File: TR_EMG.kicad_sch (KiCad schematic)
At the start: 20 parts, among them U1 INA115BU, U2 LM2904DR, U3 LM2904DR

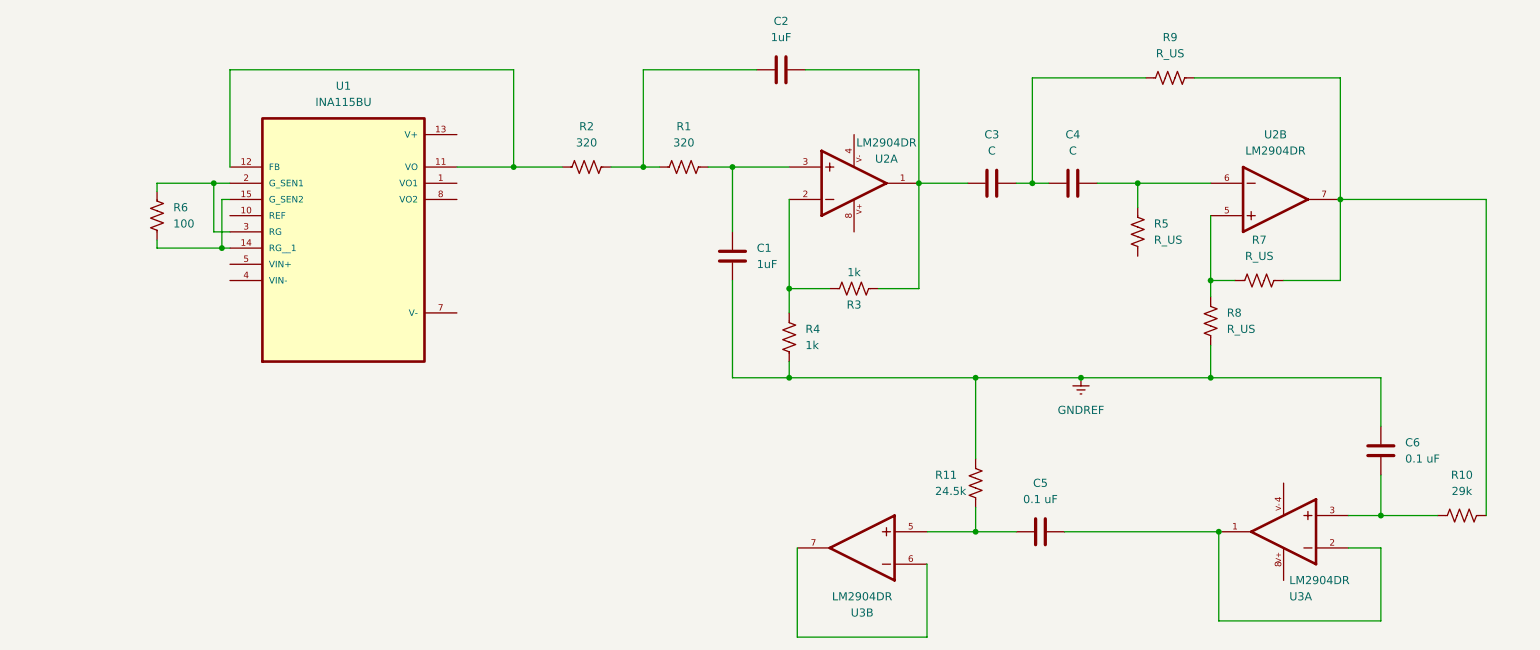
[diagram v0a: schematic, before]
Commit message: Added Hierarchy to initial design
Added hierarchy for the 2nd order lowpass and the band stop filter
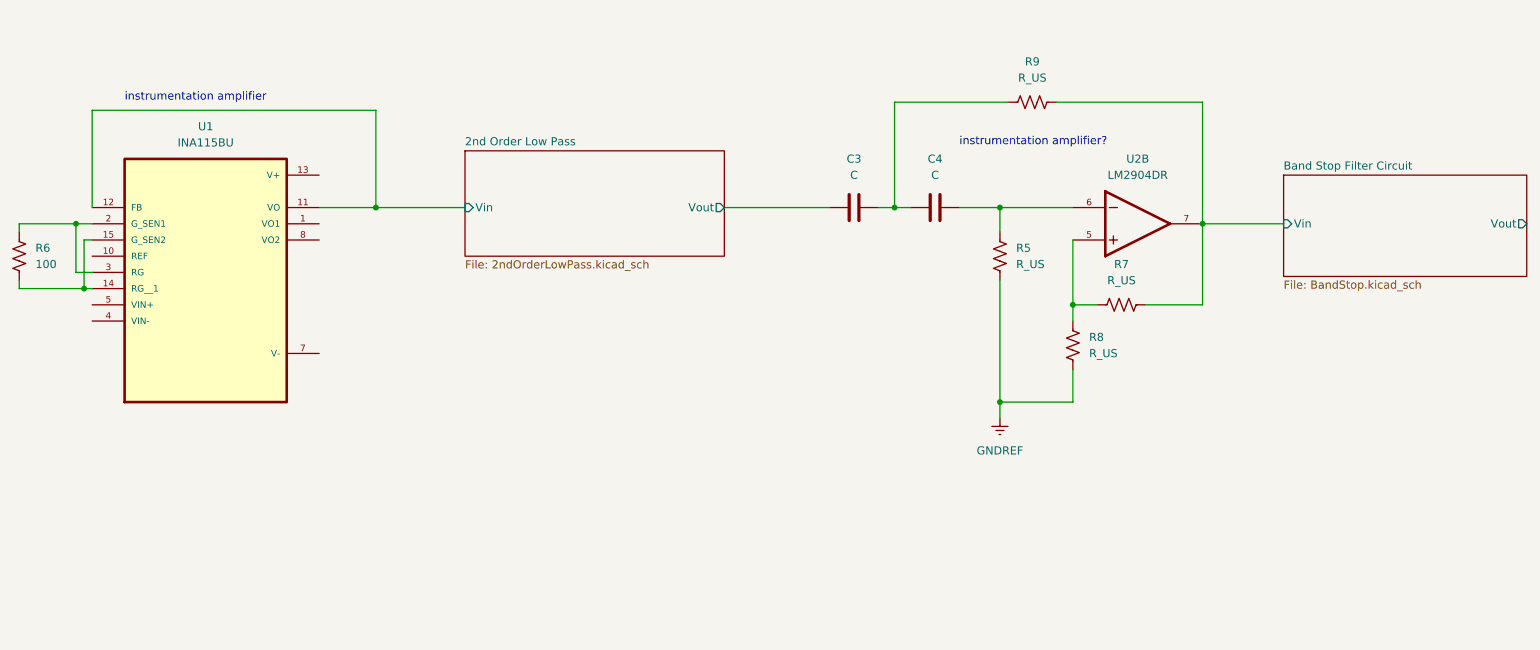
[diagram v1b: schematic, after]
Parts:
- removed C1, C2: 1uF, symbol Device:C
- removed C5, C6: 0.1 uF, symbol Device:C
- removed R1, R2: 320, symbol Device:R_US
- removed R10: 29k, symbol Device:R_US
- removed R11: 24.5k, symbol Device:R_US
- removed R3, R4: 1k, symbol Device:R_US
- removed unit 1 of U2
- removed U3: LM2904DR, LM2904DR:SOIC127P599X175-8N, symbol Digikey2:LM2904DR
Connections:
- net GNDREF: now also R5.2
- net Band Stop Filter Circuit/Vin: now reaches R7.2, R9.2, U2.7
- net 2nd Order Low Pass/Vin: now reaches U1.11 (VO), U1.12 (FB)
- net 2nd Order Low Pass/Vout: now reaches C3.1
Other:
- added sheet 2nd Order Low Pass (2ndOrderLowPass.kicad_sch)
- added sheet Band Stop Filter Circuit (BandStop.kicad_sch)
- note added: "instrumentation amplifier"
- note added: "instrumentation amplifier?"
- moved on the sheet: C3, C4, R5, R6, R7, R8, R9, U1, U2B

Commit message: add more hierarchical sheets for better formating (instru. amp. and HPF)
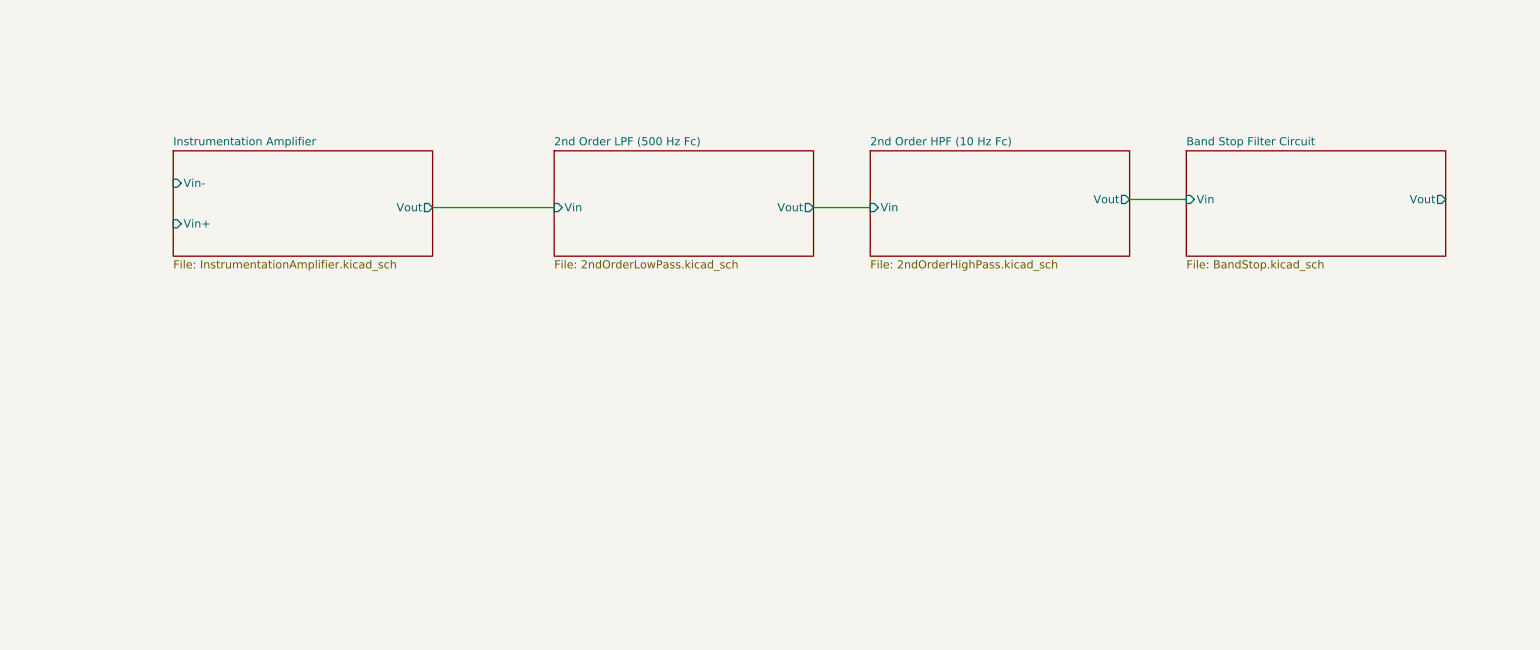
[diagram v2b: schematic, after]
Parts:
- removed C3, C4: C, symbol Device:C
- removed R5, R7, R8, R9: R_US, symbol Device:R_US
- removed R6: 100, symbol Device:R_US
- removed U1: INA115BU, INA115BU:SOIC127P1030X265-16N, symbol Digikey:INA115BU
- removed U2: LM2904DR, LM2904DR:SOIC127P599X175-8N, symbol Digikey2:LM2904DR
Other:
- sheet 2nd Order Low Pass renamed 2nd Order LPF (500 Hz Fc)
- added sheet 2nd Order HPF (10 Hz Fc) (2ndOrderHighPass.kicad_sch)
- added sheet Instrumentation Amplifier (InstrumentationAmplifier.kicad_sch)
- note removed: "instrumentation amplifier"
- note removed: "instrumentation amplifier?"
